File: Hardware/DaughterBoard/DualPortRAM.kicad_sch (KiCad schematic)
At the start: 8 parts, among them U16 74HC541, U17 74HC541, U18 74HC541, U19 74HC541, U20 AS6C62256, U21 74HC541, U22 74HC541

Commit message: Fix
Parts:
- renumbered C12 to C1, U16 to U3, U17 to U4, U18 to U5, U19 to U6, U20 to U7, U21 to U8, U22 to U9
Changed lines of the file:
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@@
   (junction (at 54.61 104.14) (diameter 1.016) (color 0 0 0 0))
   (junction (at 54.61 190.5) (diameter 1.016) (color 0 0 0 0))
+  (no_connect (at 67.31 88.9))
   (no_connect (at 109.22 20.32))
   (no_connect (at 67.31 175.26))
   (no_connect (at 194.31 30.48))
-  (no_connect (at 67.31 88.9))
   (bus_entry (at 33.02 30.48) (size 2.54 -2.54)
     (stroke (width 0.1524) (type solid) (color 0 0 0 0))
@@
   (symbol (lib_id "power:+5V") (at 54.61 62.23 0)
     (in_bom yes) (on_board yes)
-    (property "Reference" "#PWR052" (id 0) (at 54.61 66.04 0)
+    (property "Reference" "#PWR05" (id 0) (at 54.61 66.04 0)
       (effects (font (size 1.27 1.27)) hide)
     )
@@
   (symbol (lib_id "power:+5V") (at 54.61 148.59 0)
     (in_bom yes) (on_board yes)
-    (property "Reference" "#PWR054" (id 0) (at 54.61 152.4 0)
+    (property "Reference" "#PWR018" (id 0) (at 54.61 152.4 0)
       (effects (font (size 1.27 1.27)) hide)
     )
@@
   (symbol (lib_id "power:+5V") (at 72.39 19.05 0)
     (in_bom yes) (on_board yes)
-    (property "Reference" "#PWR056" (id 0) (at 72.39 22.86 0)
+    (property "Reference" "#PWR022" (id 0) (at 72.39 22.86 0)
       (effects (font (size 1.27 1.27)) hide)
     )
@@
   (symbol (lib_id "power:+5V") (at 72.39 105.41 0)
     (in_bom yes) (on_board yes)
-    (property "Reference" "#PWR058" (id 0) (at 72.39 109.22 0)
+    (property "Reference" "#PWR024" (id 0) (at 72.39 109.22 0)
       (effects (font (size 1.27 1.27)) hide)
     )
@@
   (symbol (lib_id "power:+5V") (at 157.48 30.48 0)
     (in_bom yes) (on_board yes)
-    (property "Reference" "#PWR062" (id 0) (at 157.48 34.29 0)
+    (property "Reference" "#PWR028" (id 0) (at 157.48 34.29 0)
       (effects (font (size 1.27 1.27)) hide)
     )
@@
   (symbol (lib_id "power:+5V") (at 177.8 72.898 0)
     (in_bom yes) (on_board yes)
-    (property "Reference" "#PWR060" (id 0) (at 177.8 76.708 0)
+    (property "Reference" "#PWR026" (id 0) (at 177.8 76.708 0)
       (effects (font (size 1.27 1.27)) hide)
     )
@@
   (symbol (lib_id "power:+5V") (at 224.79 27.94 0) (mirror y)
     (in_bom yes) (on_board yes)
-    (property "Reference" "#PWR065" (id 0) (at 224.79 31.75 0)
+    (property "Reference" "#PWR033" (id 0) (at 224.79 31.75 0)
       (effects (font (size 1.27 1.27)) hide)
     )
@@
   (symbol (lib_id "power:+5V") (at 224.79 86.36 0)
     (in_bom yes) (on_board yes)
-    (property "Reference" "#PWR067" (id 0) (at 224.79 90.17 0)
+    (property "Reference" "#PWR036" (id 0) (at 224.79 90.17 0)
       (effects (font (size 1.27 1.27)) hide)
     )
@@
   (symbol (lib_id "power:GND") (at 54.61 105.41 0)
     (in_bom yes) (on_board yes)
-    (property "Reference" "#PWR053" (id 0) (at 54.61 111.76 0)
+    (property "Reference" "#PWR015" (id 0) (at 54.61 111.76 0)
       (effects (font (size 1.27 1.27)) hide)
     )
@@
   (symbol (lib_id "power:GND") (at 54.61 191.77 0)
     (in_bom yes) (on_board yes)
-    (property "Reference" "#PWR055" (id 0) (at 54.61 198.12 0)
+    (property "Reference" "#PWR021" (id 0) (at 54.61 198.12 0)
       (effects (font (size 1.27 1.27)) hide)
     )
@@
   (symbol (lib_id "power:GND") (at 72.39 62.23 0)
     (in_bom yes) (on_board yes)
-    (property "Reference" "#PWR057" (id 0) (at 72.39 68.58 0)
+    (property "Reference" "#PWR023" (id 0) (at 72.39 68.58 0)
       (effects (font (size 1.27 1.27)) hide)
     )
@@
   (symbol (lib_id "power:GND") (at 72.39 148.59 0)
     (in_bom yes) (on_board yes)
-    (property "Reference" "#PWR059" (id 0) (at 72.39 154.94 0)
+    (property "Reference" "#PWR025" (id 0) (at 72.39 154.94 0)
       (effects (font (size 1.27 1.27)) hide)
     )
@@
   (symbol (lib_id "power:GND") (at 157.48 78.74 0)
     (in_bom yes) (on_board yes)
-    (property "Reference" "#PWR063" (id 0) (at 157.48 85.09 0)
+    (property "Reference" "#PWR029" (id 0) (at 157.48 85.09 0)
       (effects (font (size 1.27 1.27)) hide)
     )
@@
   (symbol (lib_id "power:GND") (at 177.8 59.69 0)
     (in_bom yes) (on_board yes)
-    (property "Reference" "#PWR064" (id 0) (at 177.8 66.04 0)
+    (property "Reference" "#PWR030" (id 0) (at 177.8 66.04 0)
       (effects (font (size 1.27 1.27)) hide)
     )
@@
   (symbol (lib_id "power:GND") (at 177.8 88.138 0)
     (in_bom yes) (on_board yes)
-    (property "Reference" "#PWR061" (id 0) (at 177.8 94.488 0)
+    (property "Reference" "#PWR027" (id 0) (at 177.8 94.488 0)
       (effects (font (size 1.27 1.27)) hide)
     )
@@
   (symbol (lib_id "power:GND") (at 224.79 71.12 0) (mirror y)
     (in_bom yes) (on_board yes)
-    (property "Reference" "#PWR066" (id 0) (at 224.79 77.47 0)
+    (property "Reference" "#PWR034" (id 0) (at 224.79 77.47 0)
       (effects (font (size 1.27 1.27)) hide)
     )
@@
   (symbol (lib_id "power:GND") (at 224.79 129.54 0)
     (in_bom yes) (on_board yes)
-    (property "Reference" "#PWR068" (id 0) (at 224.79 135.89 0)
+    (property "Reference" "#PWR037" (id 0) (at 224.79 135.89 0)
       (effects (font (size 1.27 1.27)) hide)
     )
@@
   (symbol (lib_id "Device:CP") (at 177.8 80.518 0)
     (in_bom yes) (on_board yes)
-    (property "Reference" "C12" (id 0) (at 180.975 79.248 0)
+    (property "Reference" "C1" (id 0) (at 180.975 79.248 0)
       (effects (font (size 1.27 1.27)) (justify left))
     )
@@
   (symbol (lib_name "74xx:74HCT541_2") (lib_id "74xx:74HCT541") (at 54.61 83.82 0)
     (in_bom yes) (on_board yes)
-    (property "Reference" "U16" (id 0) (at 46.99 63.5 0))
+    (property "Reference" "U3" (id 0) (at 46.99 63.5 0))
     (property "Value" "74HC541" (id 1) (at 46.99 66.04 0))
     (property "Footprint" "Package_DIP:DIP-20_W7.62mm" (id 2) (at 54.61 83.82 0)
@@
   (symbol (lib_name "74xx:74HCT541_5") (lib_id "74xx:74HCT541") (at 54.61 170.18 0)
     (in_bom yes) (on_board yes)
-    (property "Reference" "U17" (id 0) (at 46.99 149.86 0))
+    (property "Reference" "U4" (id 0) (at 46.99 149.86 0))
     (property "Value" "74HC541" (id 1) (at 46.99 152.4 0))
     (property "Footprint" "Package_DIP:DIP-20_W7.62mm" (id 2) (at 54.61 170.18 0)
@@
   (symbol (lib_name "74xx:74HCT541_1") (lib_id "74xx:74HCT541") (at 72.39 40.64 0)
     (in_bom yes) (on_board yes)
-    (property "Reference" "U18" (id 0) (at 64.77 20.32 0))
+    (property "Reference" "U5" (id 0) (at 64.77 20.32 0))
     (property "Value" "74HC541" (id 1) (at 64.77 22.86 0))
     (property "Footprint" "Package_DIP:DIP-20_W7.62mm" (id 2) (at 72.39 40.64 0)
@@
   (symbol (lib_name "74xx:74HCT541_4") (lib_id "74xx:74HCT541") (at 72.39 127 0)
     (in_bom yes) (on_board yes)
-    (property "Reference" "U19" (id 0) (at 64.77 106.68 0))
+    (property "Reference" "U6" (id 0) (at 64.77 106.68 0))
     (property "Value" "74HC541" (id 1) (at 64.77 109.22 0))
     (property "Footprint" "Package_DIP:DIP-20_W7.62mm" (id 2) (at 72.39 127 0)
@@
   (symbol (lib_name "74xx:74HCT541_6") (lib_id "74xx:74HCT541") (at 224.79 49.53 0) (mirror y)
     (in_bom yes) (on_board yes)
-    (property "Reference" "U21" (id 0) (at 232.41 29.21 0))
+    (property "Reference" "U8" (id 0) (at 232.41 29.21 0))
     (property "Value" "74HC541" (id 1) (at 232.41 31.75 0))
     (property "Footprint" "Package_DIP:DIP-20_W7.62mm" (id 2) (at 224.79 49.53 0)
@@
   (symbol (lib_name "74xx:74HCT541_3") (lib_id "74xx:74HCT541") (at 224.79 107.95 0)
     (in_bom yes) (on_board yes)
-    (property "Reference" "U22" (id 0) (at 217.17 87.63 0))
+    (property "Reference" "U9" (id 0) (at 217.17 87.63 0))
     (property "Value" "74HC541" (id 1) (at 217.17 90.17 0))
     (property "Footprint" "Package_DIP:DIP-20_W7.62mm" (id 2) (at 224.79 107.95 0)
@@
   (symbol (lib_id "Memory_RAM:HM62256BLP") (at 157.48 54.61 0)
     (in_bom yes) (on_board yes)
-    (property "Reference" "U20" (id 0) (at 157.48 52.705 0))
+    (property "Reference" "U7" (id 0) (at 157.48 52.705 0))
     (property "Value" "AS6C62256" (id 1) (at 157.48 55.245 0))
     (property "Footprint" "Package_DIP:DIP-28_W15.24mm" (id 2) (at 157.48 57.15 0)

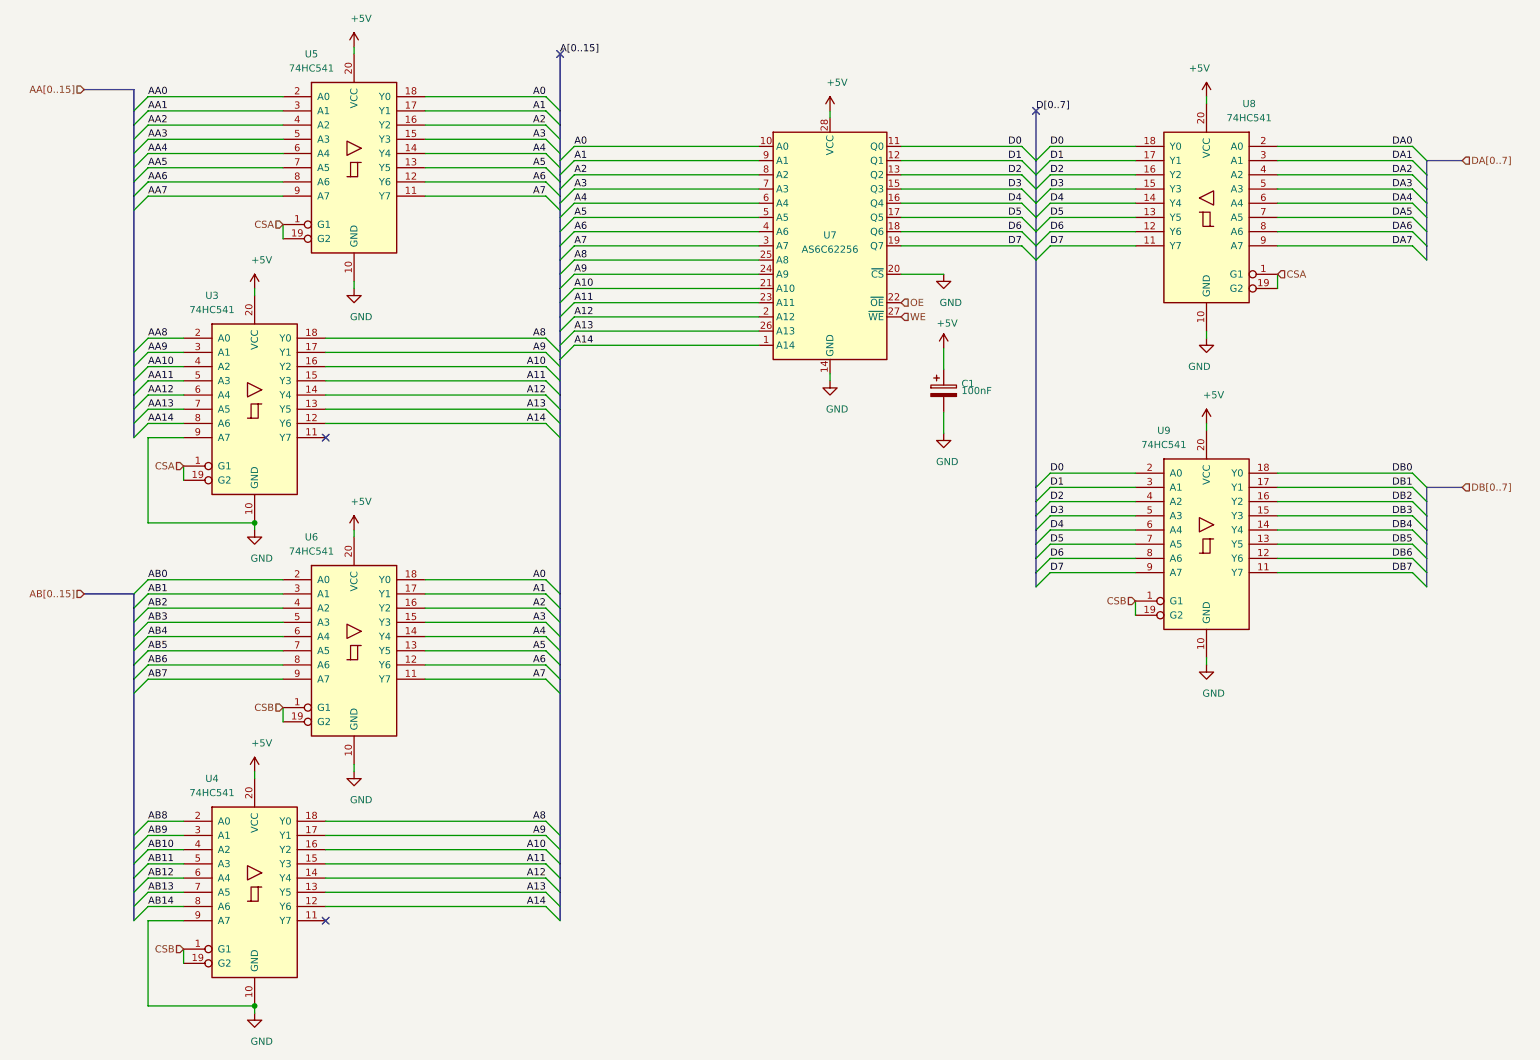
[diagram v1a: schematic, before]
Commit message: Update to Kicad 6.0
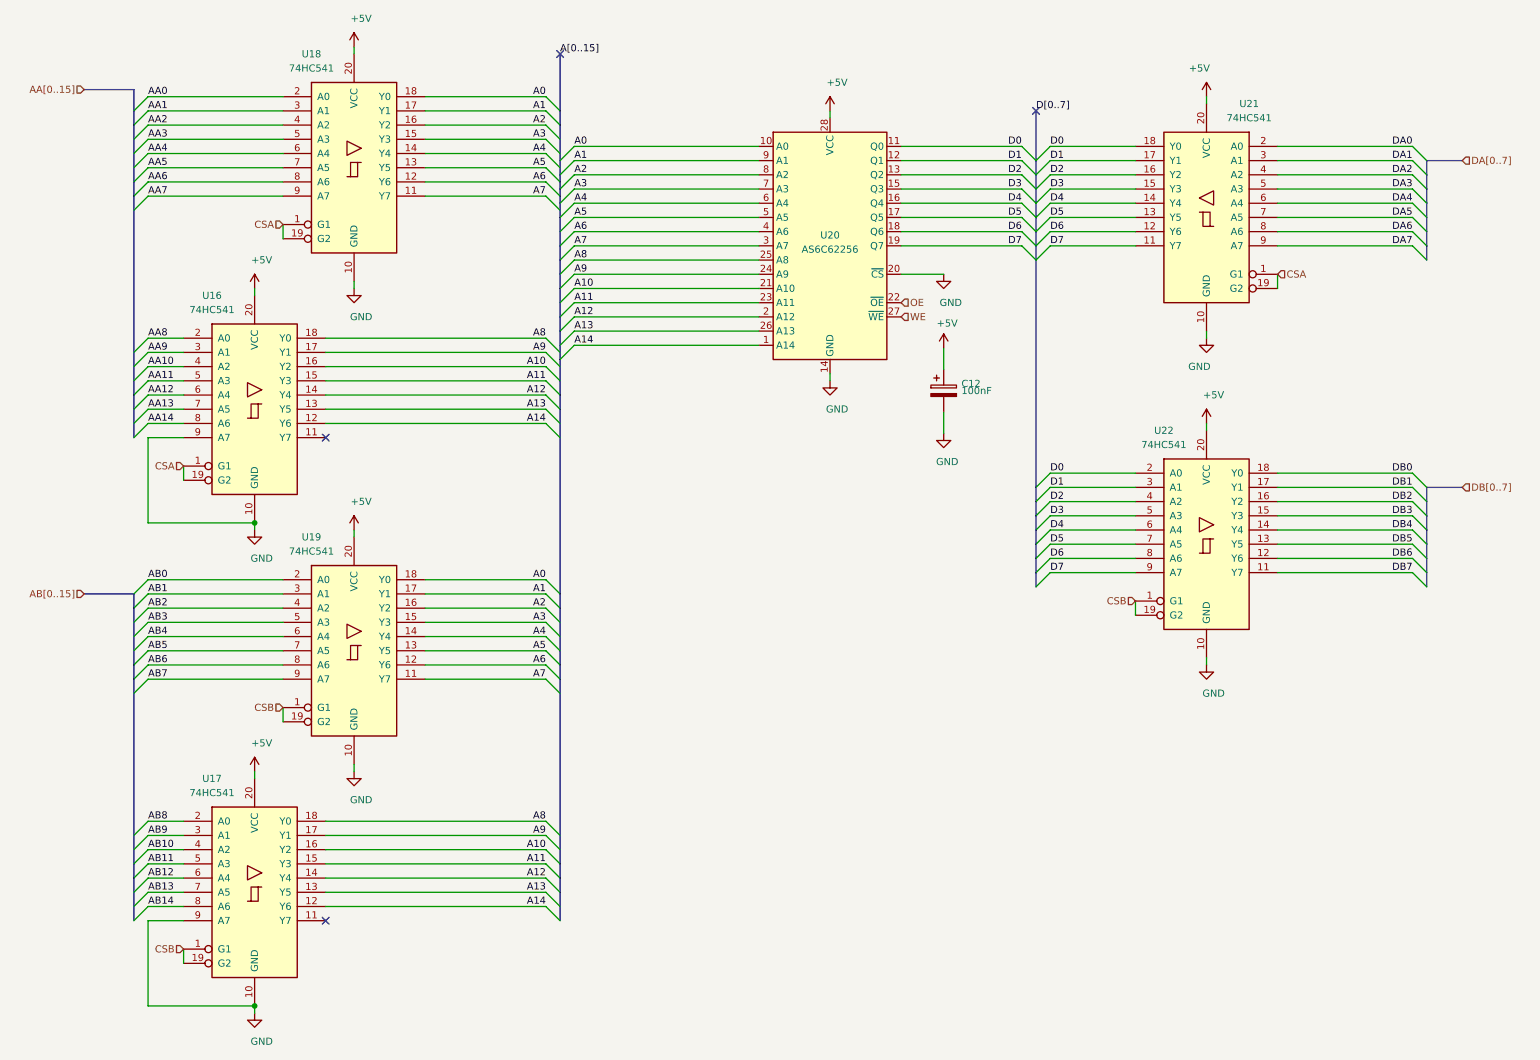
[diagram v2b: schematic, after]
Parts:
- renumbered C1 to C12, U3 to U16, U4 to U17, U5 to U18, U6 to U19, U7 to U20, U8 to U21, U9 to U22
